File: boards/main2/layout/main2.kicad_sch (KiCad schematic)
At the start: 33 parts, among them IC1 STM32H725RGV6

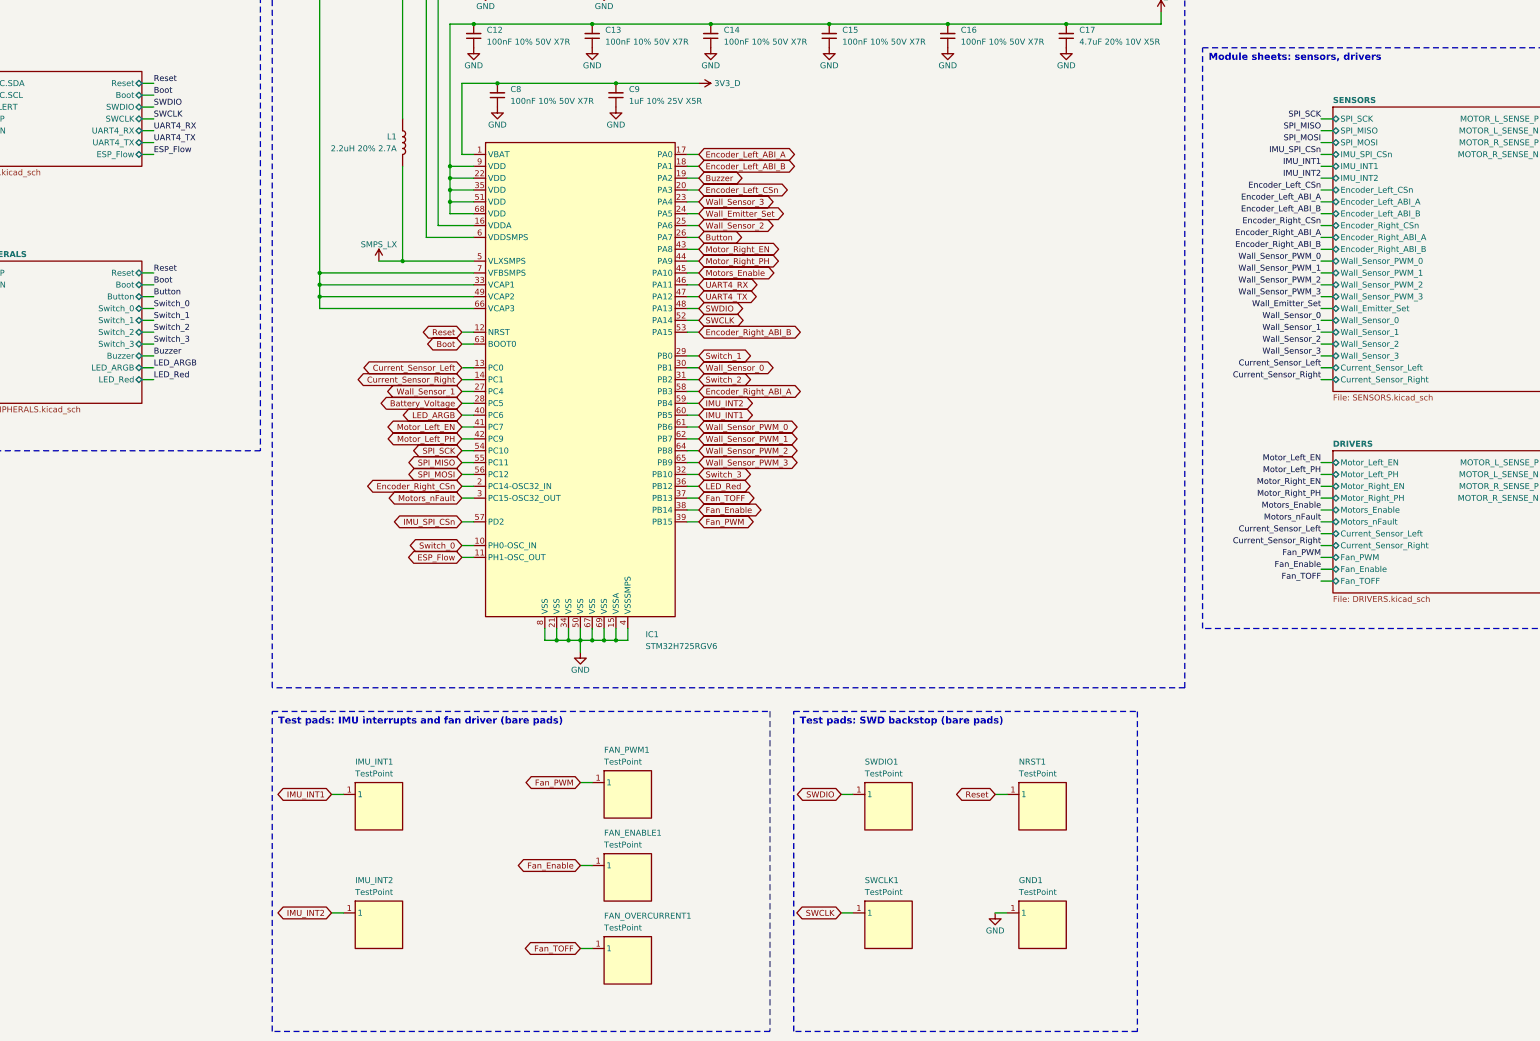
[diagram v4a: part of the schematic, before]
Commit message: 🚧 Place and route main2 but for 12 connections
place.py places every part and route.py pours the planes and routes the board, with hand-routed
fixes on top. 12 connections are still open (boards/main2/layout/README.md, Layout), so DRC and
the layout check fail on them; every other gate passes.
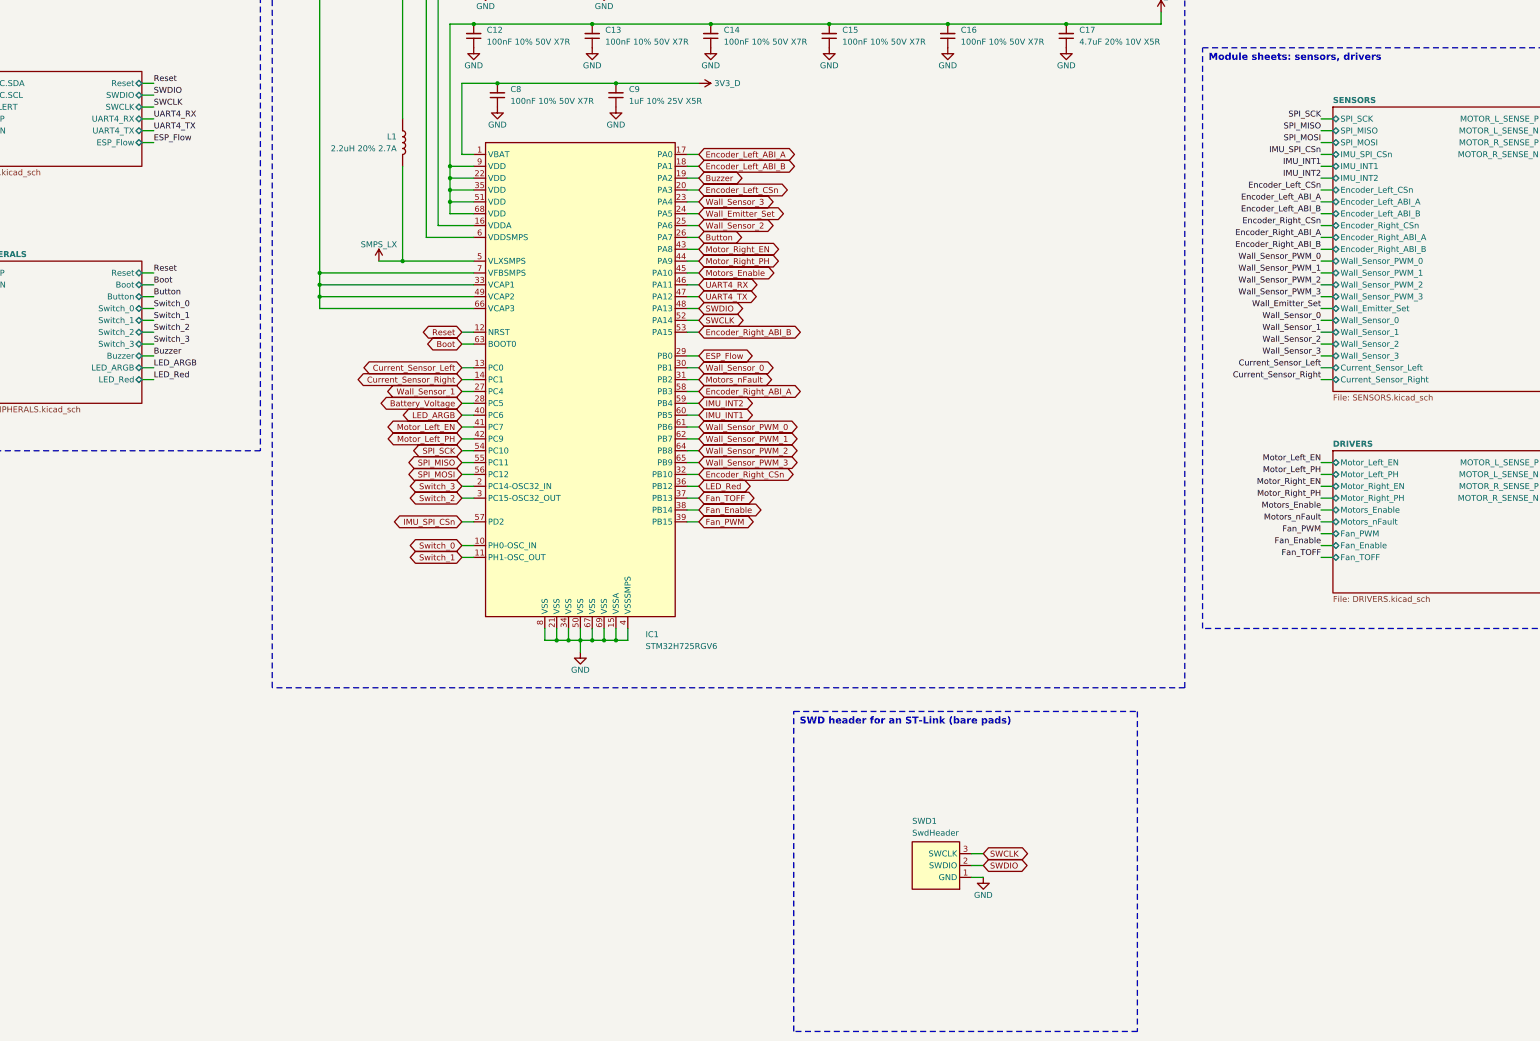
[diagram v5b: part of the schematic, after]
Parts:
- removed FAN_ENABLE1, FAN_OVERCURRENT1, FAN_PWM1, GND1, IMU_INT1, IMU_INT2, NRST1, SWCLK1, SWDIO1: TestPoint, Team-Micras_MicrasPCB_components_micras_TestPoint:TestPoint_Pad_D0.8mm, symbol TestPoint
- added SWD1: SwdHeader, Team-Micras_MicrasPCB_components_micras_SwdHeader:PinHeader_1x03_P1.27mm_Vertical, symbol SwdHeader
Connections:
- net ESP_Flow: now also IC1.29 (PB0); no longer IC1.11 (PH1-OSC_OUT)
- net Encoder_Right_CSn: now also IC1.32 (PB10); no longer IC1.2 (PC14-OSC32_IN)
- net GND: now also SWD1.1 (GND)
- net Motors_nFault: now also IC1.31 (PB2); no longer IC1.3 (PC15-OSC32_OUT)
- net SWCLK: now also SWD1.3 (SWCLK)
- net SWDIO: now also SWD1.2 (SWDIO)
- net Switch_1: now also IC1.11 (PH1-OSC_OUT); no longer IC1.29 (PB0)
- net Switch_2: now also IC1.3 (PC15-OSC32_OUT); no longer IC1.31 (PB2)
- net Switch_3: now also IC1.2 (PC14-OSC32_IN); no longer IC1.32 (PB10)
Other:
- sheet DRIVERS ports: added none; removed Current_Sensor_Left, Current_Sensor_Right
- sheet ESP ports: added none; removed Boot
- note added: "SWD header for an ST-Link (bare pads)"
- note removed: "Test pads: IMU interrupts and fan driver (bare pads)"
- note removed: "Test pads: SWD backstop (bare pads)"

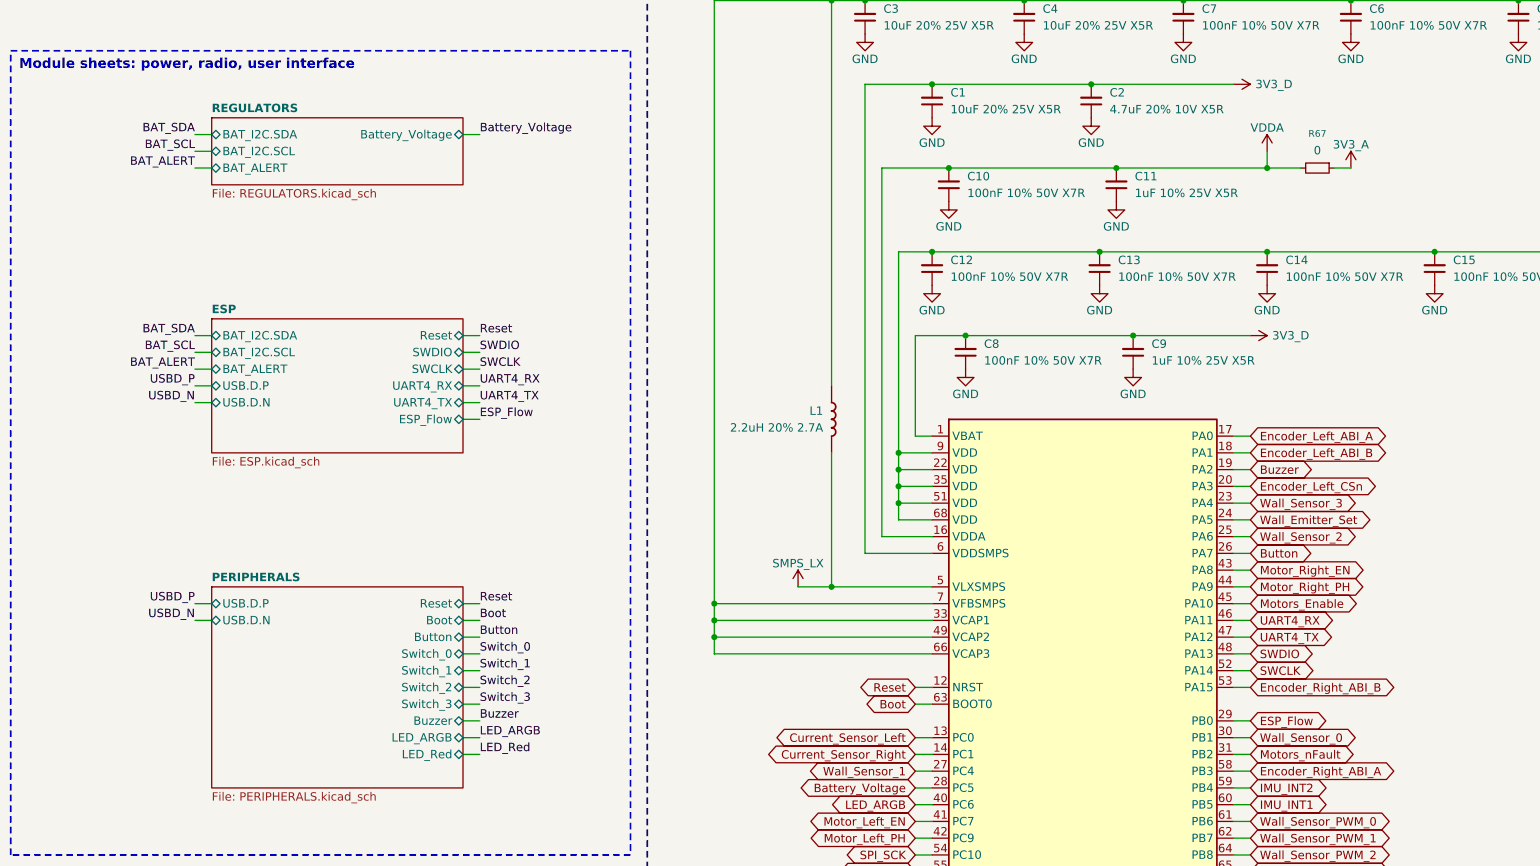
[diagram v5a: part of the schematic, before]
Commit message: ✨ Route main2 completely and fuse its battery input
- Every connection routed: short In2.Cu hops for digital STM32/ESP32 lines (never under
  switching or analog B.Cu copper, off the VBAT pour, out of the STM32 islands, In2 ground
  kept one plane), checked by a new layout test; F.Cu/B.Cu ground pours, ground stitching
  vias and teardrops.
- ADC pins swapped for the routing: Current_Sensor_Left on PB1 (fast channel), Wall_Sensor_0
  on PA4, Wall_Sensor_3 on PC0; firmware changes updated.
- Battery fuse F1 (Littelfuse 0501020.WR1, 20 A, 150 A at 32 VDC) from J1 to VBAT, the TVS and
  the switch drive behind it; the INA228 battery monitor and its shunt removed.
- route.py's DRC refills zones in KiCad, as the DRC gate does.
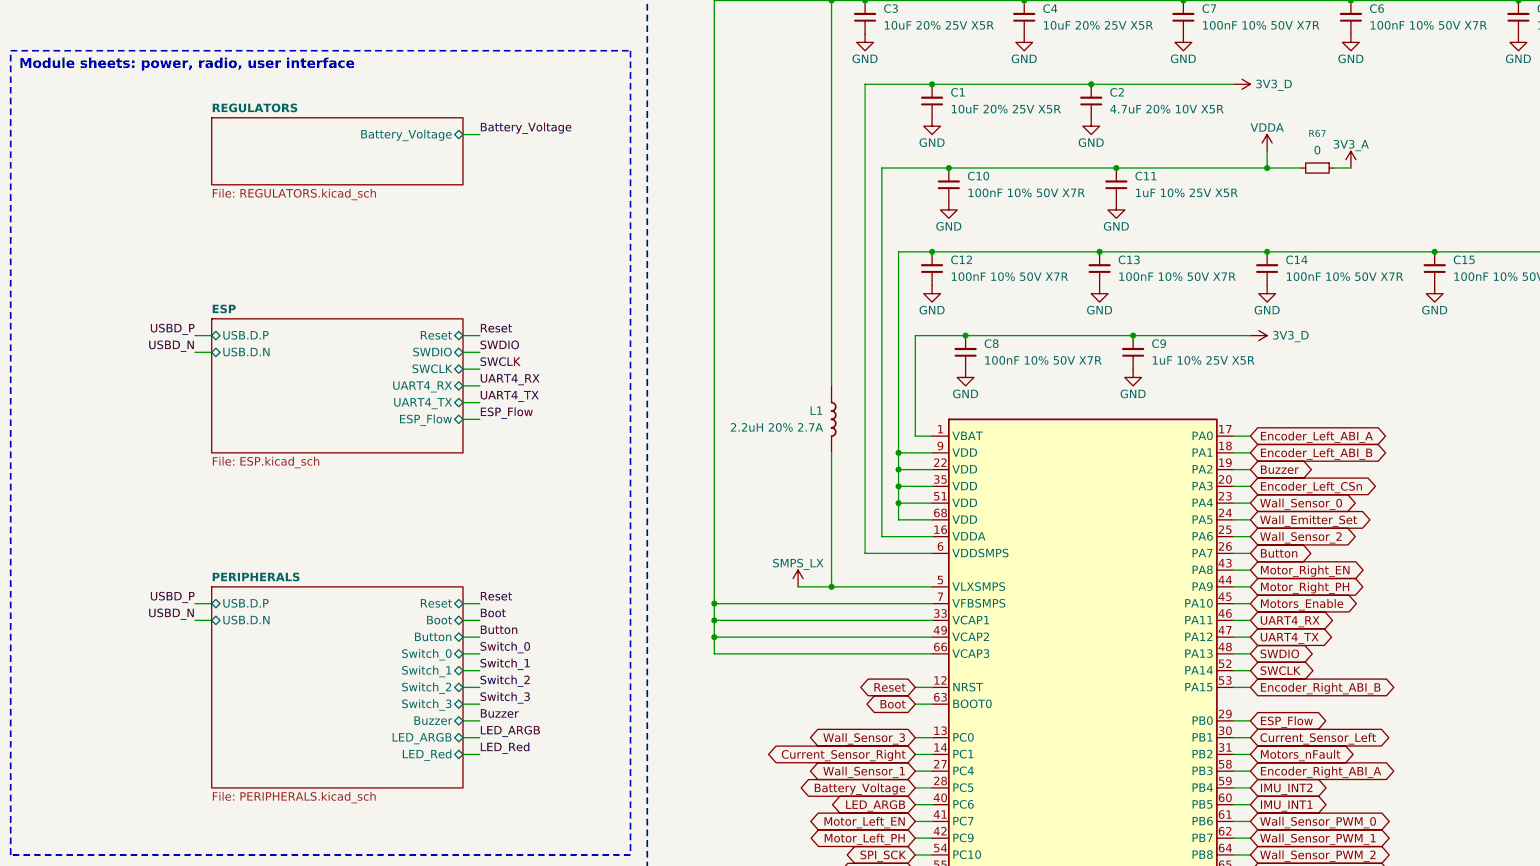
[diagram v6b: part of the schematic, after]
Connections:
- net Current_Sensor_Left: now also IC1.30 (PB1); no longer IC1.13 (PC0)
- net Wall_Sensor_0: now also IC1.23 (PA4); no longer IC1.30 (PB1)
- net Wall_Sensor_3: now also IC1.13 (PC0); no longer IC1.23 (PA4)
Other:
- sheet ESP ports: added none; removed BAT_ALERT, BAT_I2C.SCL, BAT_I2C.SDA
- sheet REGULATORS ports: added none; removed BAT_ALERT, BAT_I2C.SCL, BAT_I2C.SDA

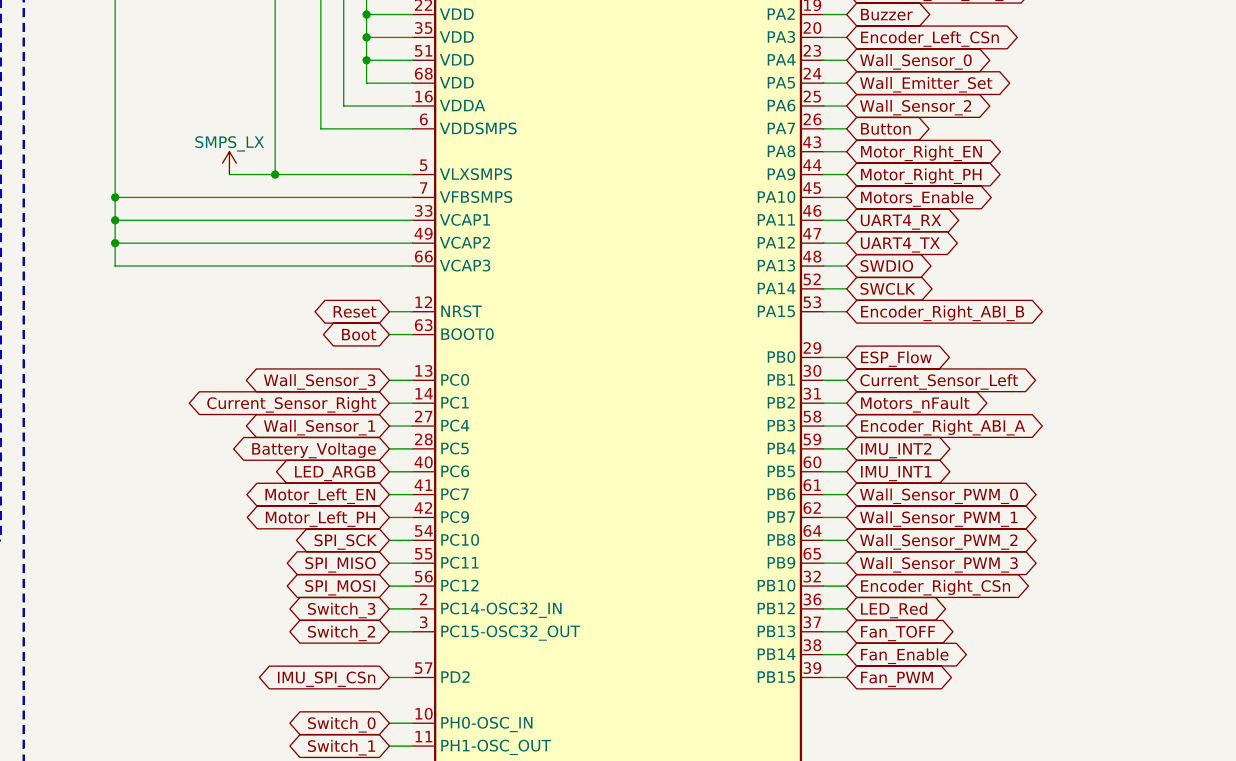
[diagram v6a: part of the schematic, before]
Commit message: 🐛 Fix main2's review findings and settle its open doubts
Schematic and parts:
- Battery input: F1 is a 12 A Littelfuse 501 (0501012.WR1). C58 now sits
  gate-source with C114 gate-drain, so Q6 stays off at plug-in. D16 clamps
  Q8's VGS. R44/R45 are 10k/2k, so VBAT can't float up on USB alone.
- Capacitors: VBAT and VSYS use 1210/0805 50 V parts, sized with Samsung's
  DC-bias curves. C109 is fitted.
- Drivers: R66/R76 are removed (the chokes are needed). ITRIP and the fan
  limit are retuned. The INA241 R_iso is 150 Ohm.
- Rails are declared as ranges, and the abs-max checks run under the TVS
  clamp.
- STM32 pin swaps for routing: the wall selectors move to TIM3,
  Motor_Left_EN to TIM8_CH2 and LED_ARGB to TIM17. CubeMX 6.18.1 confirms
  the map.
- firmware_changes.toml registers the matching firmware changes: the ADC
  0.7 us sampling time, the TIM4-triggered DAC, the fan's 50 kHz start, a
  wheel-sign self-check, VDDA tracking, contest mode, the debug halt and
  others.

Layout:
- USB D+/D- are routed as a coupled pair. The track floor is 0.12 mm.
- Stubs and detours are trimmed. The In2 VCORE/3V3_D islands are shrunk.
- The board is notched under the ESP32 antenna.
- Ground stitching, thermal reliefs, open thermal vias with split paste,
  DRV8874 heat islands and teardrops are added.
- 11 joins remain for hand-routing (layout README, Open items).

Doubts are closed by datasheets, vendor SPICE models and new research
calculations instead of bench TODOs. Tests cover each review item.
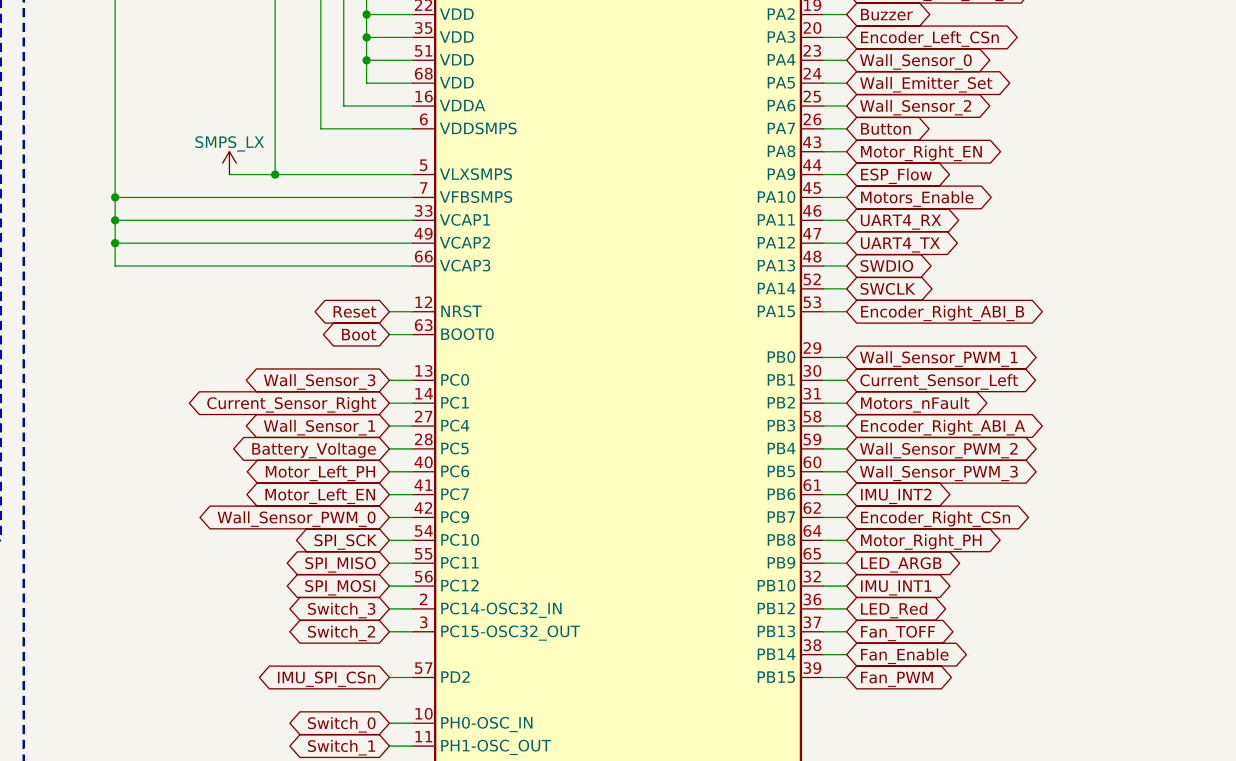
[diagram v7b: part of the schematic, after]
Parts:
- IC1: footprint Team-Micras_MicrasPCB_components_st_STM32H725RGV6:QFN-68-1EP_8x8mm_P0.4mm_EP6.5x6.5mm -> Team-Micras_MicrasPCB_components_st_STM32H725RGV6:QFN-68-1EP_8x8mm_P0.4mm_EP6.5x6.5mm_SplitPaste
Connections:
- net ESP_Flow: now also IC1.44 (PA9); no longer IC1.29 (PB0)
- net Encoder_Right_CSn: now also IC1.62 (PB7); no longer IC1.32 (PB10)
- net IMU_INT1: now also IC1.32 (PB10); no longer IC1.60 (PB5)
- net IMU_INT2: now also IC1.61 (PB6); no longer IC1.59 (PB4)
- net LED_ARGB: now also IC1.65 (PB9); no longer IC1.40 (PC6)
- net Motor_Left_PH: now also IC1.40 (PC6); no longer IC1.42 (PC9)
- net Motor_Right_PH: now also IC1.64 (PB8); no longer IC1.44 (PA9)
- net Wall_Sensor_PWM_0: now also IC1.42 (PC9); no longer IC1.61 (PB6)
- net Wall_Sensor_PWM_1: now also IC1.29 (PB0); no longer IC1.62 (PB7)
- net Wall_Sensor_PWM_2: now also IC1.59 (PB4); no longer IC1.64 (PB8)
- net Wall_Sensor_PWM_3: now also IC1.60 (PB5); no longer IC1.65 (PB9)
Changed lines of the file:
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@@
 			)
 		)
-		(property "Footprint" "Team-Micras_MicrasPCB_components_st_STM32H725RGV6:QFN-68-1EP_8x8mm_P0.4mm_EP6.5x6.5mm"
+		(property "Footprint" "Team-Micras_MicrasPCB_components_st_STM32H725RGV6:QFN-68-1EP_8x8mm_P0.4mm_EP6.5x6.5mm_SplitPaste"
 			(at 177.8 142.24 0)
 			(hide yes)
@@
 		)
 	)
-	(global_label "ESP_Flow"
+	(global_label "Wall_Sensor_PWM_1"
 		(shape bidirectional)
 		(at 203.2 137.16 0)
@@
 		)
 	)
-	(global_label "Encoder_Right_CSn"
+	(global_label "IMU_INT1"
 		(shape bidirectional)
 		(at 203.2 162.56 0)
@@
 		)
 	)
-	(global_label "LED_ARGB"
+	(global_label "Motor_Left_PH"
 		(shape bidirectional)
 		(at 152.4 149.86 180)
@@
 		)
 	)
-	(global_label "Motor_Left_PH"
+	(global_label "Wall_Sensor_PWM_0"
 		(shape bidirectional)
 		(at 152.4 154.94 180)
@@
 		)
 	)
-	(global_label "Motor_Right_PH"
+	(global_label "ESP_Flow"
 		(shape bidirectional)
 		(at 203.2 116.84 0)
@@
 		)
 	)
-	(global_label "IMU_INT2"
+	(global_label "Wall_Sensor_PWM_2"
 		(shape bidirectional)
 		(at 203.2 147.32 0)
@@
 		)
 	)
-	(global_label "IMU_INT1"
+	(global_label "Wall_Sensor_PWM_3"
 		(shape bidirectional)
 		(at 203.2 149.86 0)
@@
 		)
 	)
-	(global_label "Wall_Sensor_PWM_0"
+	(global_label "IMU_INT2"
 		(shape bidirectional)
 		(at 203.2 152.4 0)
@@
 		)
 	)
-	(global_label "Wall_Sensor_PWM_1"
+	(global_label "Encoder_Right_CSn"
 		(shape bidirectional)
 		(at 203.2 154.94 0)
@@
 		)
 	)
-	(global_label "Wall_Sensor_PWM_2"
+	(global_label "Motor_Right_PH"
 		(shape bidirectional)
 		(at 203.2 157.48 0)
@@
 		)
 	)
-	(global_label "Wall_Sensor_PWM_3"
+	(global_label "LED_ARGB"
 		(shape bidirectional)
 		(at 203.2 160.02 0)
